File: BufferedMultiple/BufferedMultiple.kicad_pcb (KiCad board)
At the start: 2 copper layers, 20.3 x 128.5 mm, 18 parts

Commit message: WIP: faceplate design
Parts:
- moved fbmhb 4.86 mm to (160.0, 163.9)
- moved Out2 3.30 mm to (157.2, 77.0)
- moved Out3 3.30 mm to (157.2, 90.9)
- moved Out5 3.30 mm to (167.8, 77.0)
- moved Out6 3.30 mm to (167.8, 90.9)
- moved In1 3.30 mm to (157.2, 49.0)
- moved In2 3.30 mm to (167.8, 49.0)
- moved Out1 3.30 mm to (157.2, 63.0)
- moved Out4 3.30 mm to (167.8, 63.0)
- moved In4 3.07 mm to (167.9, 109.5)
- moved Out12 3.07 mm to (167.9, 151.4)
- moved Out7 3.07 mm to (157.3, 123.4)
- moved In3 3.07 mm to (157.4, 109.5)
- moved Out10 3.07 mm to (167.9, 123.4)
- moved Out11 3.07 mm to (167.9, 137.4)
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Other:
- board size 20.3 x 128.5 mm -> 20.3 x 133.4 mm
- board text added: "Buffered Multiple"
- board text added: "RJModules"

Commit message: sent to production v1.0.0
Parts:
- moved Out9 5.36 mm to (157.3, 146.0)
- moved In3 5.33 mm to (157.3, 104.1)
- moved In4 5.33 mm to (167.9, 104.1)
- moved Out12 5.33 mm to (167.9, 146.0)
- moved Out11 5.33 mm to (167.9, 132.1)
- moved Out8 5.33 mm to (157.3, 132.1)
- moved Out7 5.28 mm to (157.3, 118.2)
- moved Out10 5.28 mm to (167.9, 118.2)
- moved Out3 3.40 mm to (157.3, 87.5)
- moved Out6 3.40 mm to (167.9, 87.5)
- moved fbmhb 3.36 mm to (160.0, 160.5)
- moved fpmht 3.36 mm to (159.7, 33.2)
- moved Out2 3.30 mm to (157.3, 73.7)
- moved Out5 3.30 mm to (167.9, 73.7)
- moved In1 3.30 mm to (157.3, 45.7)
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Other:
- board text added: "R-mods"
- board text removed: "RJModules"

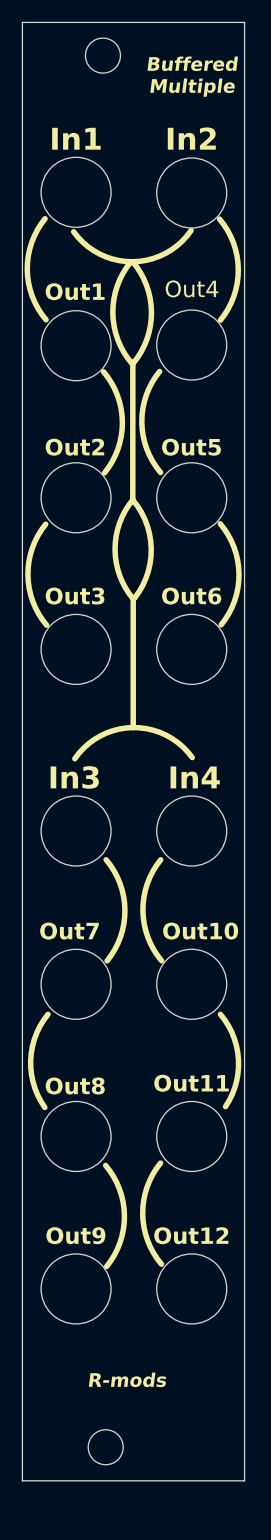
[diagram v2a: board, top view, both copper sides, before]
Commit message: fixed incorrect routing on Jheader1, moved silk screens to back layer for easy readability after assembly, oriented all jacks in the upright postition to solvealignnment descrepency in 3d model vs gerber print
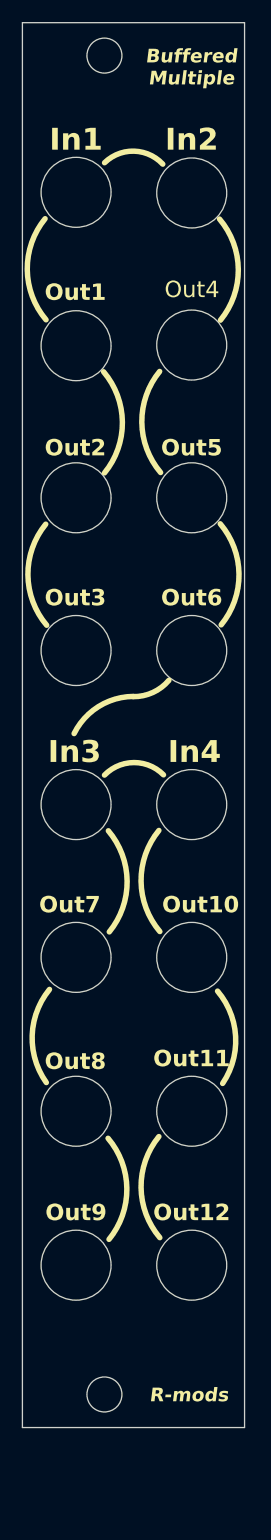
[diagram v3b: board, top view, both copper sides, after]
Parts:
- moved fbmhb 4.83 mm to (159.9, 155.7)
- moved Out10 2.46 mm to (167.9, 115.7)
- moved Out7 2.46 mm to (157.3, 115.7)
- moved In3 2.42 mm to (157.3, 101.7)
- moved In4 2.42 mm to (167.9, 101.7)
- moved Out11 2.31 mm to (167.9, 129.8)
- moved Out8 2.31 mm to (157.3, 129.8)
- moved Out12 2.17 mm to (167.9, 143.9)
- moved Out9 2.17 mm to (157.3, 143.9)
- moved fpmht 0.14 mm to (159.9, 33.2)
- moved Out3 0.10 mm to (157.3, 87.6)
- moved Out6 0.10 mm to (167.9, 87.6)
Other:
- board size 20.3 x 133.4 mm -> 20.3 x 128.5 mm
